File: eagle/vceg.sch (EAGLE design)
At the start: 65 parts, among them IC1 4052N, IC2 4001N, IC3 TL074P, IC5 CA3080E, Q1 2N3906INLINE, Q2 2N3906INLINE, U1 POWER

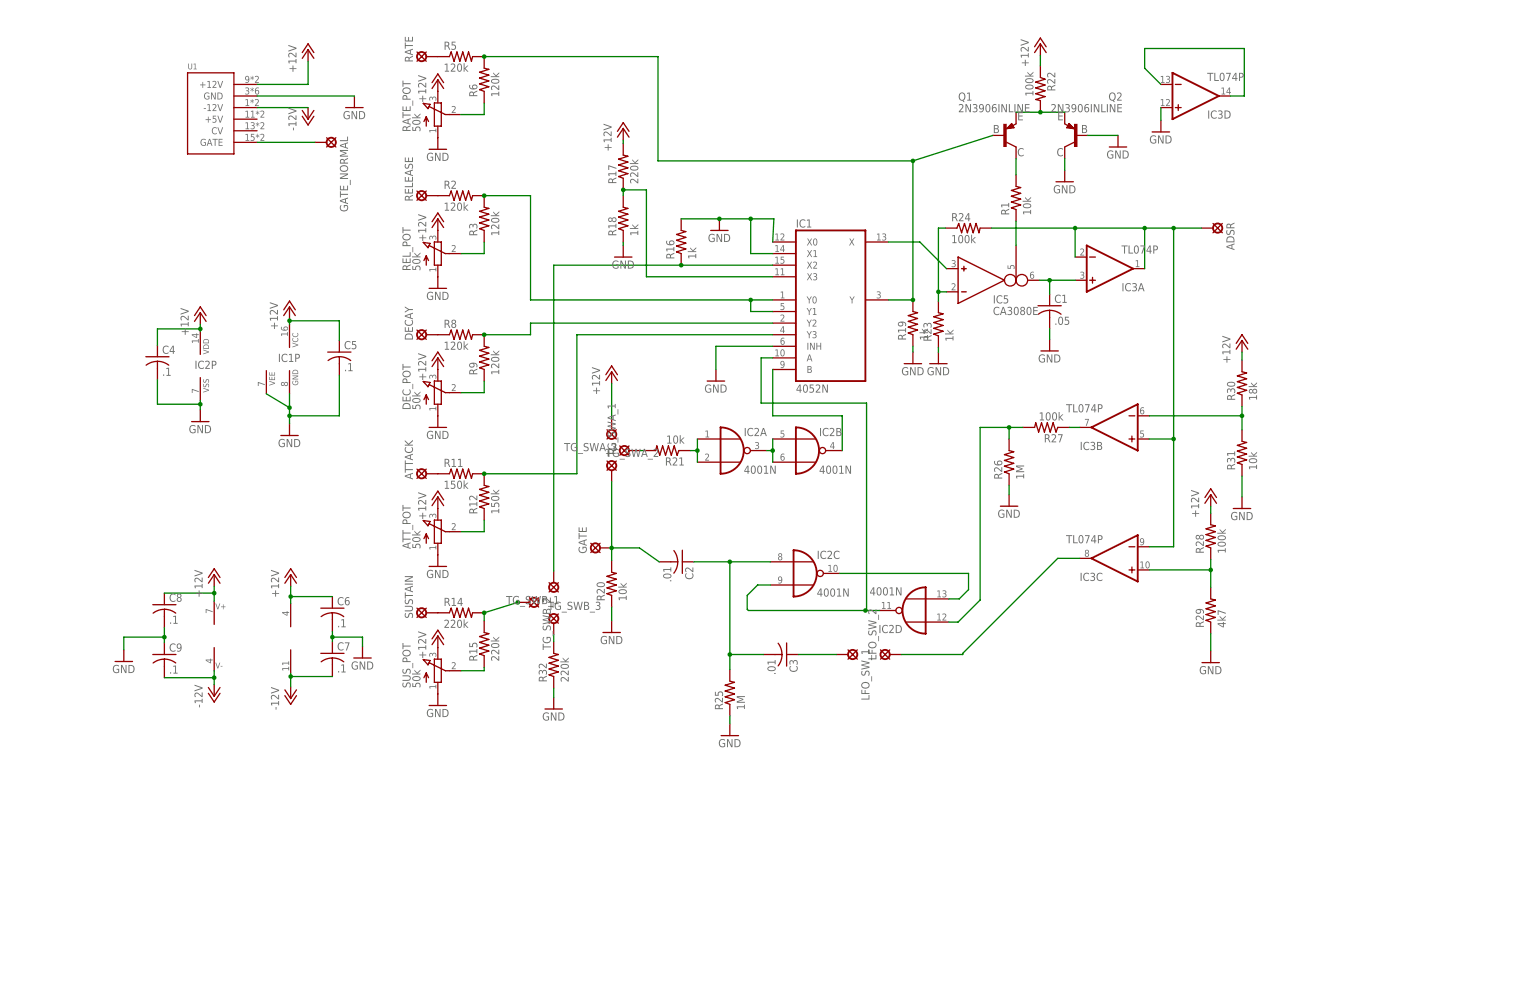
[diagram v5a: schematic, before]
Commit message: lm13700 subbed and offset mixer added
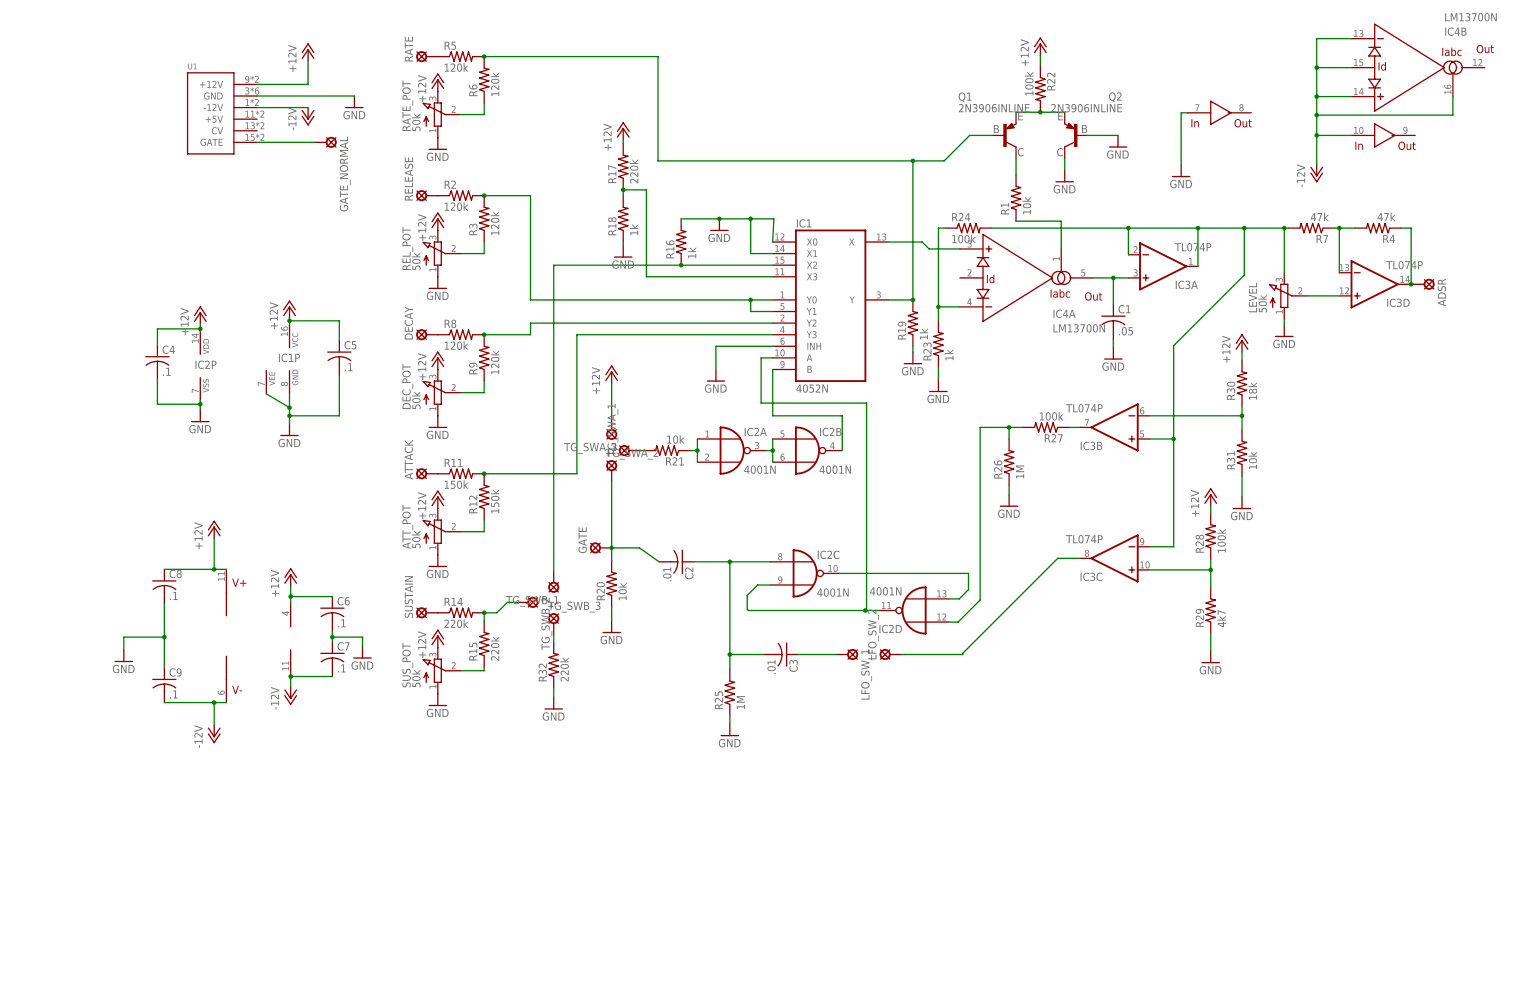
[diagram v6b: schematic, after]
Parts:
- removed IC5: CA3080E, ota:CA3080E
- added IC4: LM13700N, synthdiy:LM13700N
- added LEVEL: 50k, pot:3RP/1610N
- added R4, R7: 47k, SparkFun-Resistors:RESISTORPTH-1/4W
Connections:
- new net N$42: ADSR.MP, IC3D.OUT, R4.1
- new net N$43: IC3D.-IN, R4.2, R7.1
- net +12V: now also IC4G$5.V+; no longer IC5G$2.V+
- net -12V: now also IC4B.+IN, IC4B.-IN, IC4B.IABC, IC4B.ID, IC4G$4.IN, IC4G$5.V-; no longer IC5G$2.V-
- net GND: now also IC4G$3.IN, LEVEL.A; no longer IC3D.+IN
- net N$24: now also IC4A.-IN; no longer IC5G$1.IN_N
- net N$26: now also LEVEL.E, R7.2; no longer ADSR.MP
- net N$28: now also IC4A.OUT; no longer IC5G$1.OUT
- net N$39: now also IC4A.IABC; no longer IC5G$1.I_BIAS
- net N$40: now also IC3D.+IN, LEVEL.S; no longer IC3D.-IN, IC3D.OUT
- net N$41: now also IC4A.+IN; no longer IC5G$1.IN_P
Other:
- moved on the sheet: ADSR, C1, C8, C9, IC3A, IC3D, R23

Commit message: layout with output indicator led
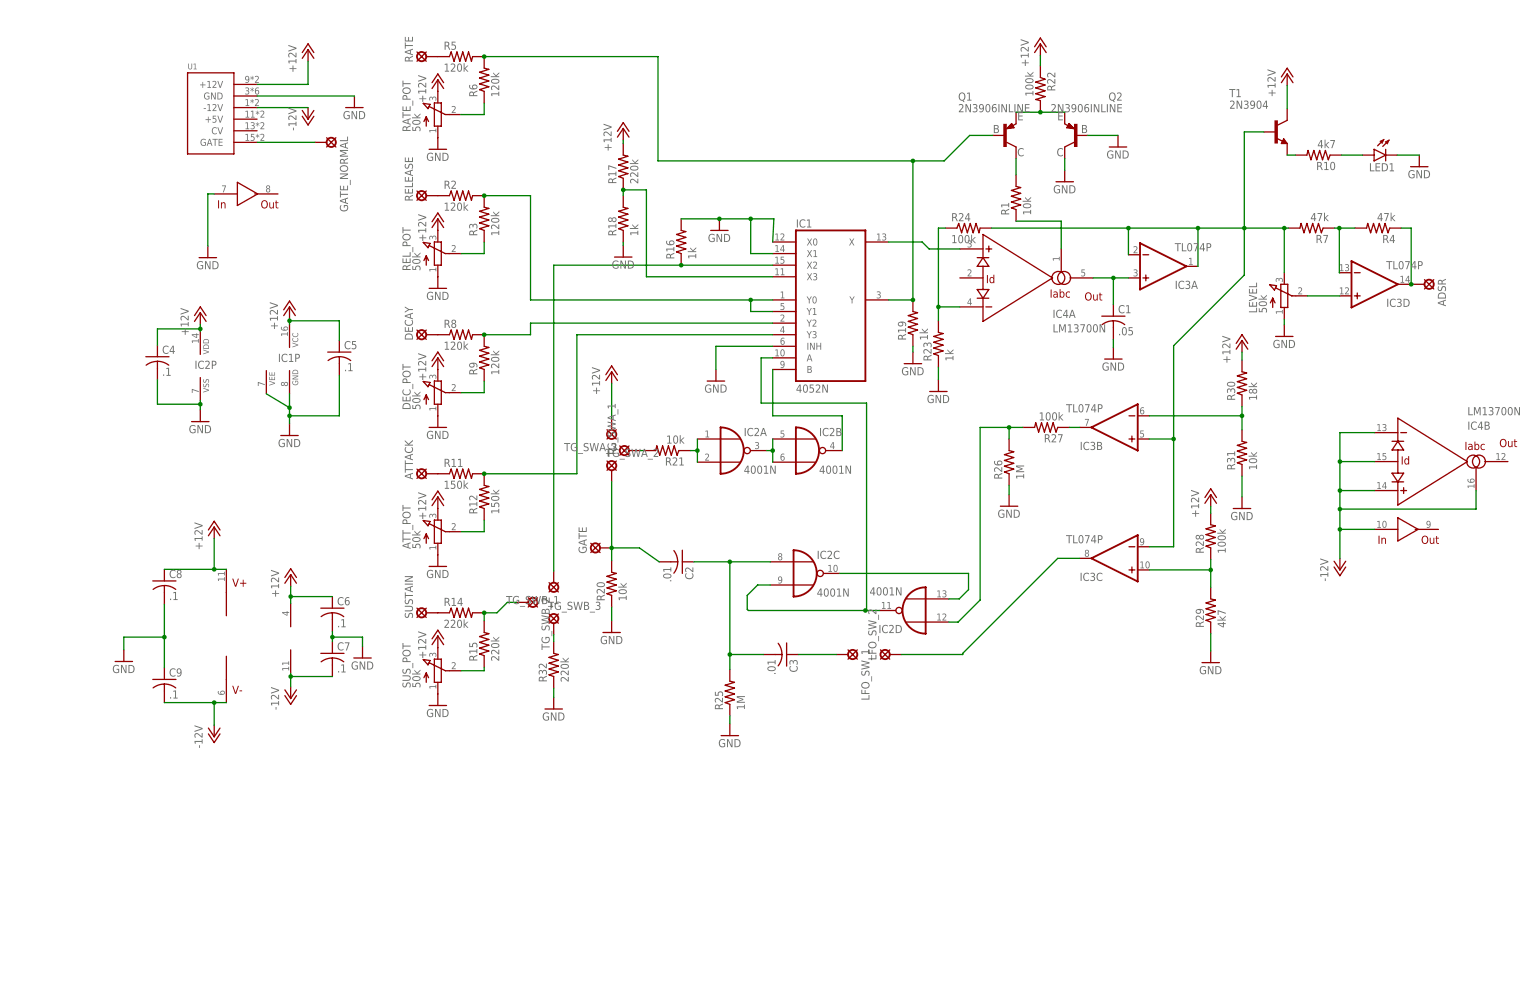
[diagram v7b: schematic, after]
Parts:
- added LED1: (no value), SparkFun-LED:LED5MM
- added R10: 4k7, SparkFun-Resistors:RESISTORPTH-1/4W
- added T1: 2N3904, transistor:2N3904
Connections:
- new net N$44: R10.2, T1.E
- new net N$45: LED1.A, R10.1
- net +12V: now also T1.C
- net GND: now also LED1.C
- net N$26: now also T1.B
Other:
- moved on the sheet: IC4B
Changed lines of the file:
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@@
 <setting verticaltext="up"/>
 </settings>
-<grid distance="0.005" unitdist="inch" unit="inch" style="lines" multiple="1" display="no" altdistance="0.01" altunitdist="inch" altunit="inch"/>
+<grid distance="0.01" unitdist="inch" unit="inch" style="lines" multiple="1" display="no" altdistance="0.01" altunitdist="inch" altunit="inch"/>
 <layers>
 <layer number="1" name="Top" color="4" fill="1" visible="no" active="no"/>
@@
 <layer number="54" name="bGND_GNDA" color="1" fill="9" visible="no" active="no"/>
 <layer number="56" name="wert" color="7" fill="1" visible="no" active="no"/>
+<layer number="57" name="tCAD" color="7" fill="1" visible="no" active="no"/>
 <layer number="90" name="Modules" color="5" fill="1" visible="yes" active="yes"/>
 <layer number="91" name="Nets" color="2" fill="1" visible="yes" active="yes"/>
@@
 <layer number="97" name="Info" color="7" fill="1" visible="yes" active="yes"/>
 <layer number="98" name="Guide" color="6" fill="1" visible="yes" active="yes"/>
+<layer number="99" name="SpiceOrder" color="7" fill="1" visible="yes" active="yes"/>
 <layer number="100" name="Muster" color="7" fill="1" visible="no" active="no"/>
 <layer number="101" name="Patch_Top" color="12" fill="4" visible="yes" active="yes"/>
@@
 <layer number="106" name="bPlate" color="7" fill="1" visible="yes" active="yes"/>
 <layer number="107" name="Crop" color="7" fill="1" visible="yes" active="yes"/>
+<layer number="108" name="tplace-old" color="10" fill="1" visible="yes" active="yes"/>
+<layer number="109" name="ref-old" color="11" fill="1" visible="yes" active="yes"/>
+<layer number="110" name="fp0" color="7" fill="1" visible="yes" active="yes"/>
+<layer number="111" name="LPC17xx" color="7" fill="1" visible="yes" active="yes"/>
+<layer number="112" name="tSilk" color="7" fill="1" visible="yes" active="yes"/>
 <layer number="116" name="Patch_BOT" color="9" fill="4" visible="yes" active="yes"/>
 <layer number="121" name="_tsilk" color="7" fill="1" visible="yes" active="yes"/>
 <layer number="122" name="_bsilk" color="7" fill="1" visible="yes" active="yes"/>
+<layer number="123" name="tTestmark" color="7" fill="1" visible="yes" active="yes"/>
+<layer number="124" name="bTestmark" color="7" fill="1" visible="yes" active="yes"/>
 <layer number="125" name="_tNames" color="7" fill="1" visible="yes" active="yes"/>
+<layer number="126" name="_bNames" color="7" fill="1" visible="yes" active="yes"/>
+<layer number="127" name="_tValues" color="7" fill="1" visible="yes" active="yes"/>
+<layer number="128" name="_bValues" color="7" fill="1" visible="yes" active="yes"/>
+<layer number="131" name="tAdjust" color="7" fill="1" visible="yes" active="yes"/>
+<layer number="132" name="bAdjust" color="7" fill="1" visible="yes" active="yes"/>
 <layer number="144" name="Drill_legend" color="7" fill="1" visible="yes" active="yes"/>
+<layer number="150" name="Notes" color="7" fill="1" visible="yes" active="yes"/>
 <layer number="151" name="HeatSink" color="7" fill="1" visible="yes" active="yes"/>
+<layer number="152" name="_bDocu" color="7" fill="1" visible="yes" active="yes"/>
+<layer number="153" name="FabDoc1" color="7" fill="1" visible="yes" active="yes"/>
+<layer number="154" name="FabDoc2" color="7" fill="1" visible="yes" active="yes"/>
+<layer number="155" name="FabDoc3" color="7" fill="1" visible="yes" active="yes"/>
+<layer number="199" name="Contour" color="7" fill="1" visible="yes" active="yes"/>
 <layer number="200" name="200bmp" color="1" fill="10" visible="yes" active="yes"/>
 <layer number="201" name="201bmp" color="2" fill="10" visible="yes" active="yes"/>
@@
 <layer number="232" name="Eagle3D_PG2" color="14" fill="2" visible="yes" active="yes"/>
 <layer number="233" name="Eagle3D_PG3" color="14" fill="4" visible="yes" active="yes"/>
+<layer number="248" name="Housing" color="7" fill="1" visible="yes" active="yes"/>
+<layer number="249" name="Edge" color="7" fill="1" visible="yes" active="yes"/>
 <layer number="250" name="Descript" color="3" fill="1" visible="no" active="no"/>
 <layer number="251" name="SMDround" color="12" fill="11" visible="no" active="no"/>
@@
 <part name="GND26" library="supply1" deviceset="GND" device=""/>
 <part name="P-4" library="supply1" deviceset="-12V" device=""/>
+<part name="T1" library="transistor" deviceset="2N3904" device=""/>
+<part name="R10" library="SparkFun-Resistors" deviceset="RESISTOR" device="PTH-1/4W" value="4k7"/>
+<part name="GND27" library="supply1" deviceset="GND" device=""/>
+<part name="LED1" library="SparkFun-LED" deviceset="LED" device="5MM"/>
+<part name="P+16" library="supply1" deviceset="+12V" device=""/>
 </parts>
 <sheets>
@@
 <instance part="R4" gate="G$1" x="278.765" y="114.046" rot="R180"/>
 <instance part="R7" gate="G$1" x="264.16" y="114.046" rot="R180"/>
-<instance part="IC4" gate="G$3" x="243.967" y="139.319"/>
-<instance part="IC4" gate="G$4" x="279.908" y="134.366"/>
-<instance part="GND26" gate="1" x="235.585" y="125.349"/>
-<instance part="IC4" gate="B" x="282.448" y="149.225"/>
-<instance part="P-4" gate="1" x="265.303" y="125.476"/>
+<instance part="IC4" gate="G$3" x="30.607" y="121.539"/>
+<instance part="IC4" gate="G$4" x="284.988" y="48.006"/>
+<instance part="GND26" gate="1" x="22.225" y="107.569"/>
+<instance part="IC4" gate="B" x="287.528" y="62.865"/>
+<instance part="P-4" gate="1" x="270.383" y="39.116"/>
+<instance part="T1" gate="G1" x="256.286" y="135.128"/>
+<instance part="R10" gate="G$1" x="265.684" y="130.048" rot="R180"/>
+<instance part="GND27" gate="1" x="287.782" y="127.508"/>
+<instance part="LED1" gate="G$1" x="277.876" y="130.048" rot="MR270"/>
+<instance part="P+16" gate="1" x="258.826" y="147.828"/>
 </instances>
 <busses>
@@
 <pinref part="GND26" gate="1" pin="GND"/>
 <pinref part="IC4" gate="G$3" pin="IN"/>
-<wire x1="236.982" y1="139.319" x2="235.585" y2="139.319" width="0.1524" layer="91"/>
-<wire x1="235.585" y1="139.319" x2="235.585" y2="127.889" width="0.1524" layer="91"/>
+<wire x1="23.622" y1="121.539" x2="22.225" y2="121.539" width="0.1524" layer="91"/>
+<wire x1="22.225" y1="121.539" x2="22.225" y2="110.109" width="0.1524" layer="91"/>
+</segment>
+<segment>
+<pinref part="GND27" gate="1" pin="GND"/>
+<pinref part="LED1" gate="G$1" pin="C"/>
+<wire x1="282.956" y1="130.048" x2="287.782" y2="130.048" width="0.1524" layer="91"/>
 </segment>
 </net>
@@
 <junction x="20.574" y="91.948"/>
 </segment>
+<segment>
+<pinref part="T1" gate="G1" pin="C"/>
+<pinref part="P+16" gate="1" pin="+12V"/>
+<wire x1="258.826" y1="145.288" x2="258.826" y2="140.208" width="0.1524" layer="91"/>
+</segment>
 </net>
 <net name="-12V" class="0">
@@
 </segment>
 <segment>
-<wire x1="272.923" y1="155.575" x2="265.303" y2="155.575" width="0.1524" layer="91"/>
-<wire x1="265.303" y1="155.575" x2="265.303" y2="149.225" width="0.1524" layer="91"/>
+<wire x1="278.003" y1="69.215" x2="270.383" y2="69.215" width="0.1524" layer="91"/>
+<wire x1="270.383" y1="69.215" x2="270.383" y2="62.865" width="0.1524" layer="91"/>
 <pinref part="P-4" gate="1" pin="-12V"/>
 <pinref part="IC4" gate="G$4" pin="IN"/>
-<wire x1="265.303" y1="149.225" x2="265.303" y2="142.875" width="0.1524" layer="91"/>
-<wire x1="265.303" y1="142.875" x2="265.303" y2="138.811" width="0.1524" layer="91"/>
-<wire x1="265.303" y1="138.811" x2="265.303" y2="134.366" width="0.1524" layer="91"/>
-<wire x1="265.303" y1="134.366" x2="265.303" y2="128.016" width="0.1524" layer="91"/>
-<wire x1="272.923" y1="134.366" x2="265.303" y2="134.366" width="0.1524" layer="91"/>
-<junction x="265.303" y="134.366"/>
+<wire x1="270.383" y1="62.865" x2="270.383" y2="56.515" width="0.1524" layer="91"/>
+<wire x1="270.383" y1="56.515" x2="270.383" y2="52.451" width="0.1524" layer="91"/>
+<wire x1="270.383" y1="52.451" x2="270.383" y2="48.006" width="0.1524" layer="91"/>
+<wire x1="270.383" y1="48.006" x2="270.383" y2="41.656" width="0.1524" layer="91"/>
+<wire x1="278.003" y1="48.006" x2="270.383" y2="48.006" width="0.1524" layer="91"/>
+<junction x="270.383" y="48.006"/>
 <pinref part="IC4" gate="B" pin="+IN"/>
-<wire x1="272.923" y1="142.875" x2="265.303" y2="142.875" width="0.1524" layer="91"/>
-<junction x="265.303" y="142.875"/>
+<wire x1="278.003" y1="56.515" x2="270.383" y2="56.515" width="0.1524" layer="91"/>
+<junction x="270.383" y="56.515"/>
 <pinref part="IC4" gate="B" pin="ID"/>
-<wire x1="265.303" y1="149.225" x2="272.923" y2="149.225" width="0.1524" layer="91"/>
-<junction x="265.303" y="149.225"/>
+<wire x1="270.383" y1="62.865" x2="278.003" y2="62.865" width="0.1524" layer="91"/>
+<junction x="270.383" y="62.865"/>
 <pinref part="IC4" gate="B" pin="-IN"/>
 <pinref part="IC4" gate="B" pin="IABC"/>
-<wire x1="295.148" y1="142.875" x2="295.148" y2="138.811" width="0.1524" layer="91"/>
-<wire x1="295.148" y1="138.811" x2="265.303" y2="138.811" width="0.1524" layer="91"/>
-<junction x="265.303" y="138.811"/>
+<wire x1="300.228" y1="56.515" x2="300.228" y2="52.451" width="0.1524" layer="91"/>
+<wire x1="300.228" y1="52.451" x2="270.383" y2="52.451" width="0.1524" layer="91"/>
+<junction x="270.383" y="52.451"/>
 </segment>
 </net>
@@
 <pinref part="R7" gate="G$1" pin="2"/>
 <pinref part="LEVEL" gate="G$1" pin="E"/>
+<pinref part="T1" gate="G1" pin="B"/>
+<wire x1="253.746" y1="135.128" x2="249.428" y2="135.128" width="0.1524" layer="91"/>
+<wire x1="249.428" y1="135.128" x2="249.428" y2="114.046" width="0.1524" layer="91"/>
 </segment>
 </net>
@@
 </segment>
 </net>
+<net name="N$44" class="0">
+<segment>
+<pinref part="T1" gate="G1" pin="E"/>
+<pinref part="R10" gate="G$1" pin="2"/>
+<wire x1="260.604" y1="130.048" x2="258.826" y2="130.048" width="0.1524" layer="91"/>
+</segment>
+</net>
+<net name="N$45" class="0">
+<segment>
+<pinref part="R10" gate="G$1" pin="1"/>
+<pinref part="LED1" gate="G$1" pin="A"/>
+<wire x1="275.336" y1="130.048" x2="270.764" y2="130.048" width="0.1524" layer="91"/>
+</segment>
+</net>
